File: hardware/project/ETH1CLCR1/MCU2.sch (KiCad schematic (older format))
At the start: 28 parts, among them J1301 Conn_02x05, U1301 24LC08B-E/MS, U1302 STM32H743ZI, Y1301 NX3225GD-8MHZ-STD-CRA-3

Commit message: PCB layout
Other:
- moved on the sheet: C1319, R1304
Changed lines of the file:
@@
 L Device:R R?
 U 1 1 5E806B33
-P 15200 8200
+P 14950 8200
 AR Path="/5DCED281/5E806B33" Ref="R?"  Part="1"
 AR Path="/5DF35BC8/5E806B33" Ref="R?"  Part="1"
 AR Path="/5DEACD0F/5E806B33" Ref="R1304"  Part="1"
-F 0 "R1304" H 15270 8246 50  0000 L CNN
-F 1 "10k" H 15270 8155 50  0000 L CNN
-F 2 "Resistor_SMD:R_0603_1608Metric_Pad1.05x0.95mm_HandSolder" V 15130 8200 50  0001 C CNN
-F 3 "~" H 15200 8200 50  0001 C CNN
-	1    15200 8200
+F 0 "R1304" H 15020 8246 50  0000 L CNN
+F 1 "10k" H 15020 8155 50  0000 L CNN
+F 2 "Resistor_SMD:R_0603_1608Metric_Pad1.05x0.95mm_HandSolder" V 14880 8200 50  0001 C CNN
+F 3 "~" H 14950 8200 50  0001 C CNN
+	1    14950 8200
 	1    0    0    -1
 $EndComp
@@
 L Device:C C?
 U 1 1 5E806B39
-P 15200 8600
+P 14950 8600
 AR Path="/5DCED281/5E806B39" Ref="C?"  Part="1"
 AR Path="/5DF35BC8/5E806B39" Ref="C?"  Part="1"
 AR Path="/5DEACD0F/5E806B39" Ref="C1319"  Part="1"
-F 0 "C1319" H 15315 8646 50  0000 L CNN
-F 1 "100n" H 15315 8555 50  0000 L CNN
-F 2 "Capacitor_SMD:C_0603_1608Metric_Pad1.05x0.95mm_HandSolder" H 15238 8450 50  0001 C CNN
-F 3 "~" H 15200 8600 50  0001 C CNN
-	1    15200 8600
-	1    0    0    -1
-$EndComp
-Wire Wire Line
-	15200 8400 15200 8450
-Wire Wire Line
-	15200 8350 15200 8400
-Connection ~ 15200 8400
-Wire Wire Line
-	15700 8400 15200 8400
-Text Label 15700 8400 2    50   ~ 0
+F 0 "C1319" H 15065 8646 50  0000 L CNN
+F 1 "100n" H 15065 8555 50  0000 L CNN
+F 2 "Capacitor_SMD:C_0603_1608Metric_Pad1.05x0.95mm_HandSolder" H 14988 8450 50  0001 C CNN
+F 3 "~" H 14950 8600 50  0001 C CNN
+	1    14950 8600
+	1    0    0    -1
+$EndComp
+Wire Wire Line
+	14950 8400 14950 8450
+Wire Wire Line
+	14950 8350 14950 8400
+Connection ~ 14950 8400
+Wire Wire Line
+	15450 8400 14950 8400
+Text Label 15450 8400 2    50   ~ 0
 MCU_NRST
 Wire Wire Line
@@
 	14350 6200 14300 6200
 Wire Wire Line
-	15200 8400 14300 8400
+	14950 8400 14300 8400
 NoConn ~ 2900 2600
 NoConn ~ 2900 2700
@@
 L ETH1CLCR1:DGNDF #PWR01320
 U 1 1 5E492D3A
-P 15200 8750
-F 0 "#PWR01320" H 15200 8500 50  0001 C CNN
-F 1 "DGNDF" H 15205 8577 50  0000 C CNN
-F 2 "" H 15200 8750 50  0001 C CNN
-F 3 "" H 15200 8750 50  0001 C CNN
-	1    15200 8750
+P 14950 8750
+F 0 "#PWR01320" H 14950 8500 50  0001 C CNN
+F 1 "DGNDF" H 14955 8577 50  0000 C CNN
+F 2 "" H 14950 8750 50  0001 C CNN
+F 3 "" H 14950 8750 50  0001 C CNN
+	1    14950 8750
 	1    0    0    -1
 $EndComp
@@
 L power:+3.3VP #PWR01319
 U 1 1 5E6F95E8
-P 15200 8050
-F 0 "#PWR01319" H 15350 8000 50  0001 C CNN
-F 1 "+3.3VP" H 15220 8193 50  0000 C CNN
-F 2 "" H 15200 8050 50  0001 C CNN
-F 3 "" H 15200 8050 50  0001 C CNN
-	1    15200 8050
-	1    0    0    -1
-$EndComp
+P 14950 8050
+F 0 "#PWR01319" H 15100 8000 50  0001 C CNN
+F 1 "+3.3VP" H 14970 8193 50  0000 C CNN
+F 2 "" H 14950 8050 50  0001 C CNN
+F 3 "" H 14950 8050 50  0001 C CNN
+	1    14950 8050
+	1    0    0    -1
+$EndComp

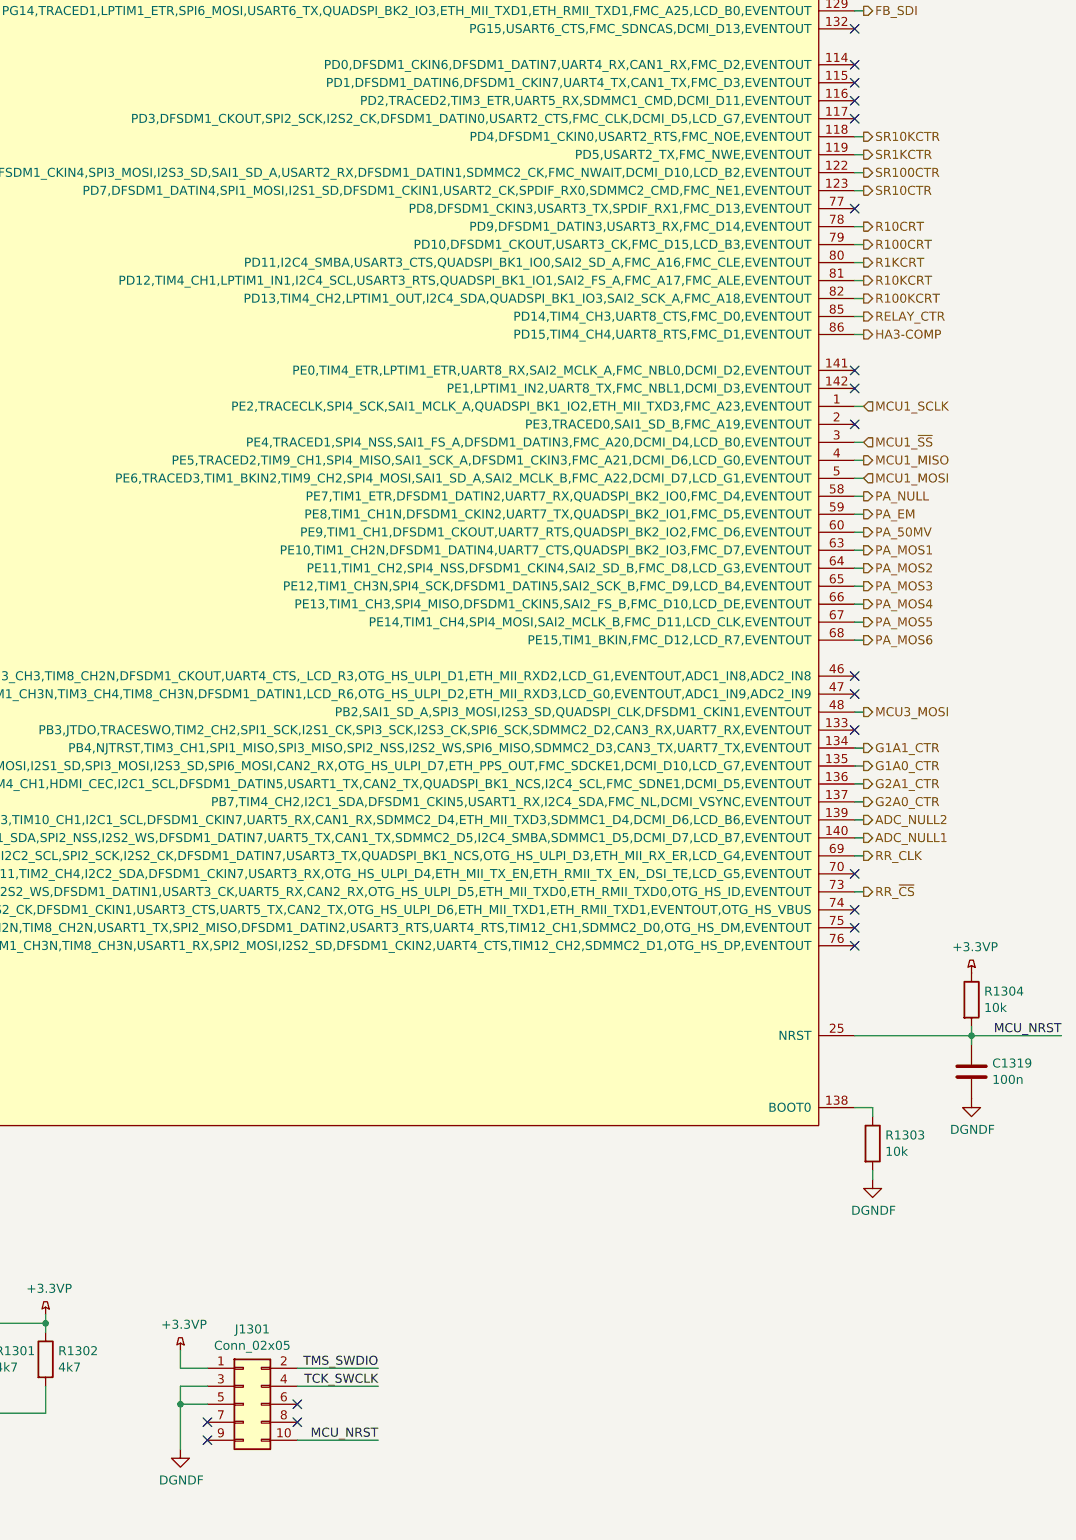
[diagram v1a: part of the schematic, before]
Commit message: Checked the schematics. Created BOM.
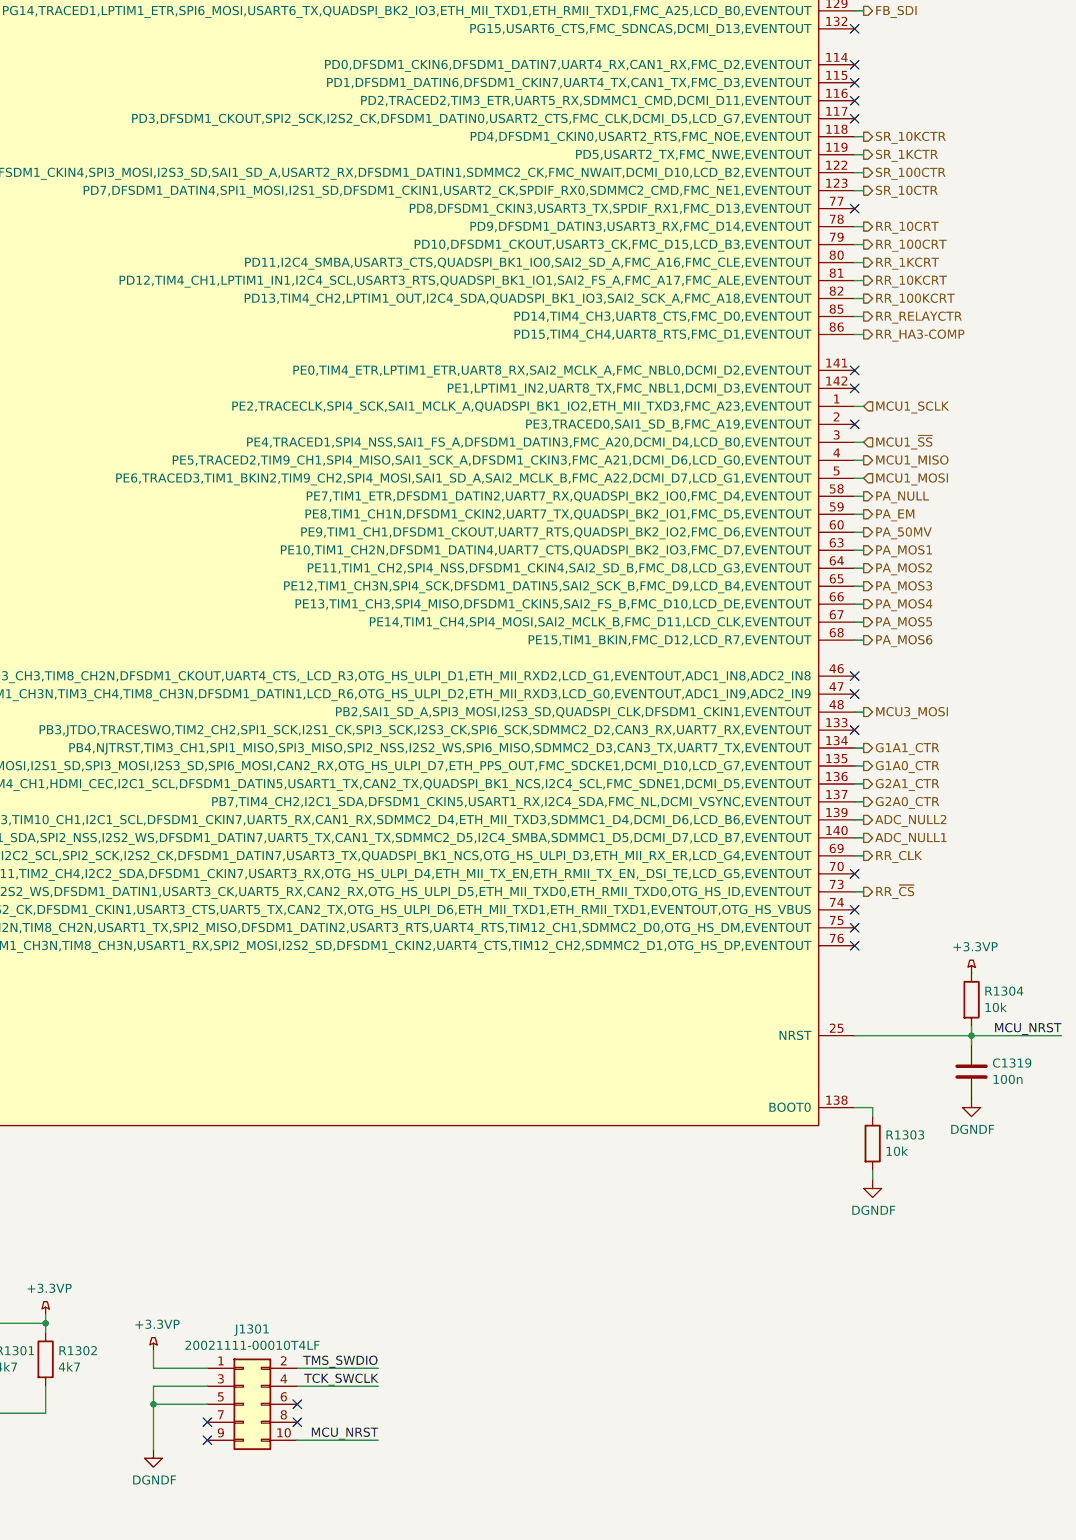
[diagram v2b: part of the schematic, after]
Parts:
- J1301: value Conn_02x05 -> 20021111-00010T4LF
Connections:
- net HA3-COMP renamed RR_HA3-COMP
- net R100CRT renamed RR_100CRT
- net R100KCRT renamed RR_100KCRT
- net R10CRT renamed RR_10CRT
- net R10KCRT renamed RR_10KCRT
- net R1KCRT renamed RR_1KCRT
- net RELAY_CTR renamed RR_RELAYCTR
- net SR100CTR renamed SR_100CTR
- net SR10CTR renamed SR_10CTR
- net SR10KCTR renamed SR_10KCTR
- net SR1KCTR renamed SR_1KCTR
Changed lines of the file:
@@
 encoding utf-8
 Sheet 13 15
-Title ""
-Date ""
-Rev ""
+Title "MCU2"
+Date "2020-01-19"
+Rev "1.0"
 Comp ""
 Comment1 ""
@@
 AR Path="/5DEACD0F/5DD8EE39" Ref="J1301"  Part="1"
 F 0 "J1301" H 10950 10867 50  0000 C CNN
-F 1 "Conn_02x05" H 10950 10776 50  0000 C CNN
+F 1 "20021111-00010T4LF" H 10950 10776 50  0000 C CNN
 F 2 "Connector_PinHeader_1.27mm:PinHeader_2x05_P1.27mm_Vertical" H 10900 10450 50  0001 C CNN
 F 3 "~" H 10900 10450 50  0001 C CNN
@@
 NoConn ~ 10700 10650
 Wire Wire Line
-	10700 10450 10550 10450
-Wire Wire Line
-	10550 10450 10550 10350
-Wire Wire Line
-	10550 10350 10700 10350
-Wire Wire Line
-	10550 10700 10550 10450
-Connection ~ 10550 10450
-Wire Wire Line
-	10550 10150 10550 10250
-Wire Wire Line
-	10550 10250 10700 10250
+	10700 10450 10400 10450
+Wire Wire Line
+	10400 10450 10400 10350
+Wire Wire Line
+	10400 10350 10700 10350
+Wire Wire Line
+	10400 10700 10400 10450
+Connection ~ 10400 10450
+Wire Wire Line
+	10400 10150 10400 10250
+Wire Wire Line
+	10400 10250 10700 10250
 Wire Wire Line
 	11200 10250 11650 10250
@@
 L ETH1CLCR1:DGNDF #PWR01317
 U 1 1 5DD90023
-P 10550 10700
-F 0 "#PWR01317" H 10550 10450 50  0001 C CNN
-F 1 "DGNDF" H 10555 10527 50  0000 C CNN
-F 2 "" H 10550 10700 50  0001 C CNN
-F 3 "" H 10550 10700 50  0001 C CNN
-	1    10550 10700
+P 10400 10700
+F 0 "#PWR01317" H 10400 10450 50  0001 C CNN
+F 1 "DGNDF" H 10405 10527 50  0000 C CNN
+F 2 "" H 10400 10700 50  0001 C CNN
+F 3 "" H 10400 10700 50  0001 C CNN
+	1    10400 10700
 	1    0    0    -1
 $EndComp
@@
 NoConn ~ 14300 6500
 Text HLabel 14350 3500 2    50   Output ~ 0
-SR1KCTR
+SR_1KCTR
 Text HLabel 14350 3400 2    50   Output ~ 0
-SR10KCTR
+SR_10KCTR
 Text HLabel 14350 3700 2    50   Output ~ 0
-SR10CTR
+SR_10CTR
 Text HLabel 14350 3600 2    50   Output ~ 0
-SR100CTR
+SR_100CTR
 Wire Wire Line
 	2850 5300 2900 5300
@@
 L power:+3.3VP #PWR01316
 U 1 1 5E705830
-P 10550 10150
-F 0 "#PWR01316" H 10700 10100 50  0001 C CNN
-F 1 "+3.3VP" H 10570 10293 50  0000 C CNN
-F 2 "" H 10550 10150 50  0001 C CNN
-F 3 "" H 10550 10150 50  0001 C CNN
-	1    10550 10150
+P 10400 10150
+F 0 "#PWR01316" H 10550 10100 50  0001 C CNN
+F 1 "+3.3VP" H 10420 10293 50  0000 C CNN
+F 2 "" H 10400 10150 50  0001 C CNN
+F 3 "" H 10400 10150 50  0001 C CNN
+	1    10400 10150
 	1    0    0    -1
 $EndComp
@@
 CXN_REL3
 Text HLabel 14350 4000 2    50   Output ~ 0
-R100CRT
+RR_100CRT
 Text HLabel 14350 3900 2    50   Output ~ 0
-R10CRT
+RR_10CRT
 Text HLabel 14350 4100 2    50   Output ~ 0
-R1KCRT
+RR_1KCRT
 Text HLabel 14350 4200 2    50   Output ~ 0
-R10KCRT
+RR_10KCRT
 Text HLabel 14350 4300 2    50   Output ~ 0
-R100KCRT
+RR_100KCRT
 Text HLabel 14350 4400 2    50   Output ~ 0
-RELAY_CTR
+RR_RELAYCTR
 Text HLabel 14350 4500 2    50   Output ~ 0
-HA3-COMP
+RR_HA3-COMP
 Text HLabel 14350 5400 2    50   Output ~ 0
 PA_NULL

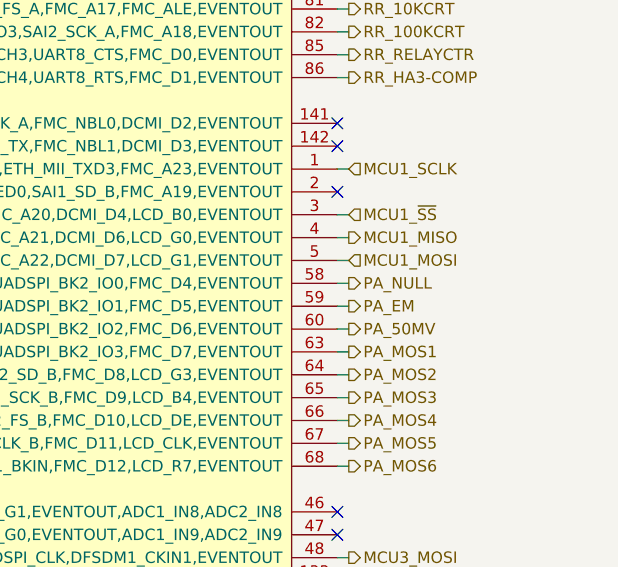
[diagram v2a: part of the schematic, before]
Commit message: Fixed some mistakes in the foorpeints. BOM list ready.
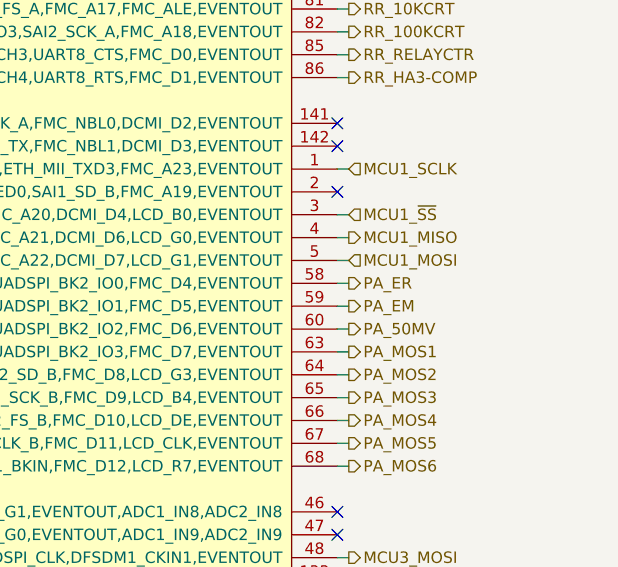
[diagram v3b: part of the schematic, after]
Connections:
- net PA_NULL renamed PA_ER
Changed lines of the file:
@@
 RR_HA3-COMP
 Text HLabel 14350 5400 2    50   Output ~ 0
-PA_NULL
+PA_ER
 Text HLabel 14350 5500 2    50   Output ~ 0
 PA_EM

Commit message: PCB layout
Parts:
- added C1318: 100n, Capacitor_SMD:C_0603_1608Metric_Pad1.05x0.95mm_HandSolder, symbol Device:C
- renumbered C1318 to C1319, C1319 to C1320, U1302 to U1301, U1301 to U1302
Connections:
- net +3.3VP: now also C1318.1
- net DGNDF: now also C1318.2
- net MCU1_STATUS_IN2: now reaches U1301.10 (PF0,I2C2_SDA,FMC_A0,EVENTOUT)
- net MCU1_STATUS_IN renamed MCU1_STATUS_IN1
- no-connect marks 45 -> 44
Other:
- moved on the sheet: C1319, FB1301, R1301, R1302, U1302

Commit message: PCB layout
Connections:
- net CXN_REL1: now also U1301.49 (PF11,SAI1_SD_A,SPI3_MOSI,I2S3_SD,QUADSPI_CLK,DFSDM1_CKIN1,EVENTOUT); no longer U1301.87 (PG2,FMC_A12,EVENTOUT)
- net CXN_REL2: now also U1301.48 (PB2,SAI1_SD_A,SPI3_MOSI,I2S3_SD,QUADSPI_CLK,DFSDM1_CKIN1,EVENTOUT); no longer U1301.88 (PG3,FMC_A13,EVENTOUT)
- net CXN_REL3: now also U1301.47 (PB1,TIM1_CH3N,TIM3_CH4,TIM8_CH3N,DFSDM1_DATIN1,LCD_R6,OTG_HS_ULPI_D2,ETH_MII_RXD3,LCD_G0,EVENTOUT,ADC1_IN9,ADC2_IN9); no longer U1301.89 (PG4,FMC_A14,FMC_BA0,EVENTOUT)
- net CXN_REL4: now also U1301.46 (PB0,TIM1_CH2N,TIM3_CH3,TIM8_CH2N,DFSDM1_CKOUT,UART4_CTS,_LCD_R3,OTG_HS_ULPI_D1,ETH_MII_RXD2,LCD_G1,EVENTOUT,ADC1_IN8,ADC2_IN8); no longer U1301.90 (PG5,FMC_A15,FMC_BA1,EVENTOUT)
- net CXN_REL5: now also U1301.45 (PC5,DFSDM1_DATIN2,SPDIF_RX3,ETH_MII_RXD1,ETH_RMII_RXD1,FMC_SDCKE0,EVENTOUT,ADC1_IN15,ADC2_IN15); no longer U1301.91 (PG6,FMC_NE3,DCMI_D12,LCD_R7,EVENTOUT)
- net CXN_REL6: now also U1301.44 (PC4,DFSDM1_CKIN2,I2S1_MCK,SPDIF_RX2,ETH_MII_RXD0,ETH_RMII_RXD0,FMC_SDNE0,EVENTOUT,ADC1_IN14,ADC2_IN14); no longer U1301.92 (PG7,SAI1_MCLK_A,USART6_CK,FMC_INT,DCMI_D13,LCD_CLK,EVENTOUT)
- net MCU3_MOSI: now also U1301.113 (PC12,TRACED3,SPI3_MOSI,I2S3_SD,USART3_CK,UART5_TX,SDMMC1_CK,DCMI_D9,EVENTOUT); no longer U1301.48 (PB2,SAI1_SD_A,SPI3_MOSI,I2S3_SD,QUADSPI_CLK,DFSDM1_CKIN1,EVENTOUT)
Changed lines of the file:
@@
 	14950 8400 14300 8400
 NoConn ~ 2900 2600
-NoConn ~ 2900 2700
 NoConn ~ 2900 2800
 NoConn ~ 2900 3300
@@
 Wire Wire Line
 	2850 8600 2900 8600
-NoConn ~ 14300 6500
 Text HLabel 14350 3500 2    50   Output ~ 0
 SR_1KCTR
@@
 	1    0    0    -1
 $EndComp
-Text HLabel 14350 1500 2    50   Output ~ 0
-CXN_REL1
-Text HLabel 14350 1600 2    50   Output ~ 0
-CXN_REL2
-Text HLabel 14350 1700 2    50   Output ~ 0
-CXN_REL3
+Text HLabel 2850 5400 0    50   Output ~ 0
+CXN_REL6
+Text HLabel 2850 5500 0    50   Output ~ 0
+CXN_REL5
+Text HLabel 14350 6400 2    50   Output ~ 0
+CXN_REL4
 Text HLabel 14350 4000 2    50   Output ~ 0
 RR_100CRT
@@
 Wire Wire Line
 	14300 7300 14350 7300
-NoConn ~ 14300 6400
 NoConn ~ 14300 7900
 NoConn ~ 14300 7800
-NoConn ~ 2900 6200
-NoConn ~ 2900 5400
-NoConn ~ 2900 5500
 NoConn ~ 2900 4300
 NoConn ~ 2900 4400
@@
 	2900 4800 2850 4800
 Wire Wire Line
-	14300 6600 14350 6600
+	2900 6200 2850 6200
 Text HLabel 2850 6000 0    50   Output ~ 0
 MCU3_SCLK
 Text HLabel 2850 6100 0    50   Input ~ 0
 MCU3_MISO
-Text HLabel 14350 6600 2    50   Output ~ 0
+Text HLabel 2850 6200 0    50   Output ~ 0
 MCU3_MOSI
 Text HLabel 2850 4800 0    50   Output ~ 0
 MCU3_NSS
-Text HLabel 14350 1800 2    50   Output ~ 0
-CXN_REL4
-Text HLabel 14350 1900 2    50   Output ~ 0
-CXN_REL5
-Text HLabel 14350 2000 2    50   Output ~ 0
-CXN_REL6
+Text HLabel 14350 6500 2    50   Output ~ 0
+CXN_REL3
+Text HLabel 14350 6600 2    50   Output ~ 0
+CXN_REL2
+Text HLabel 2850 2700 0    50   Output ~ 0
+CXN_REL1
 NoConn ~ 2900 1800
 NoConn ~ 2900 1700
@@
 $EndComp
 Wire Wire Line
-	14300 1500 14350 1500
-Wire Wire Line
-	14300 1600 14350 1600
-Wire Wire Line
-	14300 1700 14350 1700
-Wire Wire Line
-	14300 1800 14350 1800
-Wire Wire Line
-	14300 1900 14350 1900
-Wire Wire Line
-	14300 2000 14350 2000
+	2900 5400 2850 5400
+Wire Wire Line
+	2900 5500 2850 5500
+Wire Wire Line
+	14300 6400 14350 6400
+Wire Wire Line
+	14300 6500 14350 6500
+Wire Wire Line
+	14300 6600 14350 6600
+Wire Wire Line
+	2900 2700 2850 2700
 $Comp
 L power:+3.3VP #PWR01303
@@
 Wire Wire Line
 	2850 1600 2900 1600
+NoConn ~ 14300 1500
+NoConn ~ 14300 1600
+NoConn ~ 14300 1700
+NoConn ~ 14300 1800
+NoConn ~ 14300 1900
+NoConn ~ 14300 2000
 $EndSCHEMATC
